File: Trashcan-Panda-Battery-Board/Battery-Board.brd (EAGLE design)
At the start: 89.9 x 38.6 mm, 4 parts, among them J1 B2B-PH-SM4-TB(LF)(SN)

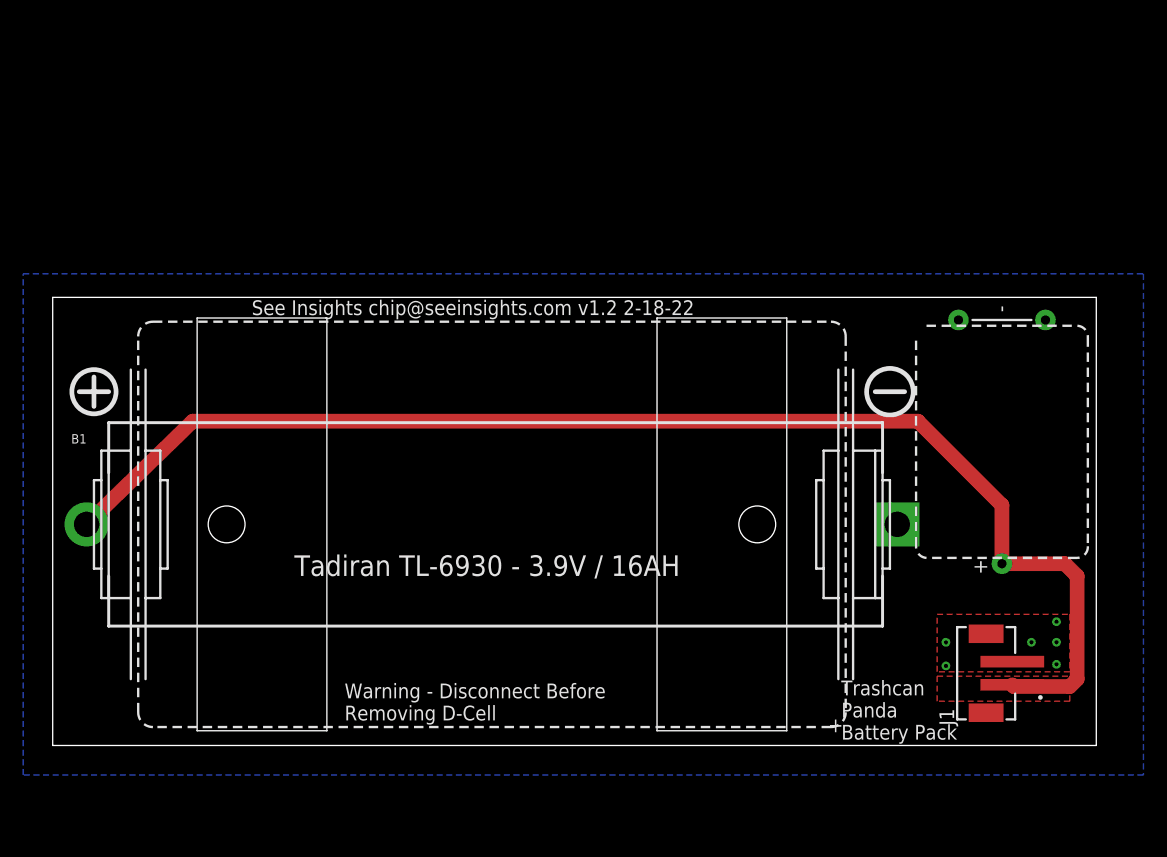
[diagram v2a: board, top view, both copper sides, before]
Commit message: Added PTC
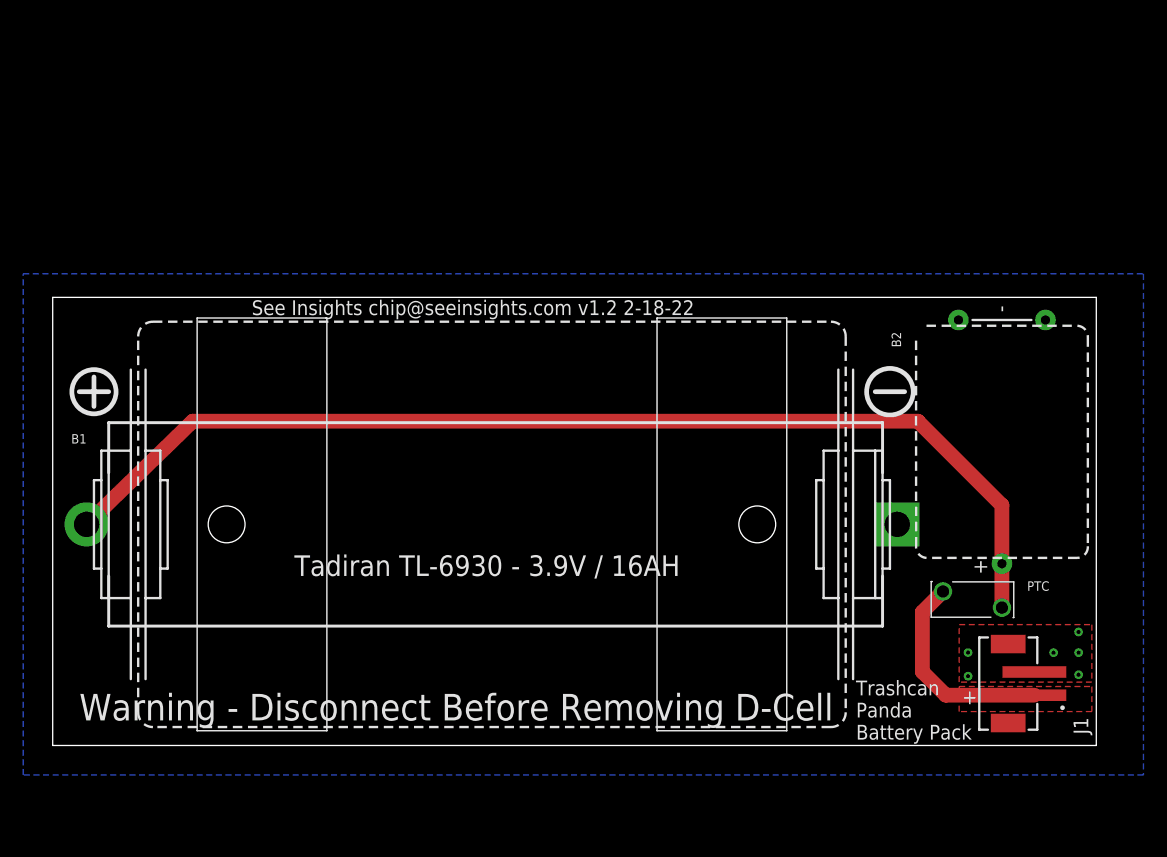
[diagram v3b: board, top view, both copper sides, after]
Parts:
- added PTC: RUSBF120, Battery-Board:PTC-RUSBF120
- moved J1 2.10 mm to (84.6, 5.33)
- renumbered U$1 to B2
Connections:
- new net V-OUT: J1.1, PTC.2
- net VCC: now also PTC.1; no longer J1.1
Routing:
- net V-OUT: track 0.00 -> 18.1 mm
- net VCC: track 112.2 -> 94.3 mm
- added copper zone on layer 1, net V-OUT
- removed copper zone on layer 1, net VCC
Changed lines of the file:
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@@
 <wire x1="89.916" y1="38.608" x2="0" y2="38.608" width="0" layer="20"/>
 <wire x1="0" y1="38.608" x2="0" y2="0" width="0" layer="20"/>
-<text x="67.945" y="0.508" size="1.27" layer="21">Trashcan
+<text x="69.215" y="0.508" size="1.27" layer="21">Trashcan
 Panda
 Battery Pack</text>
-<text x="25.146" y="2.159" size="1.27" layer="21">Warning - Disconnect Before
-Removing D-Cell</text>
+<text x="2.286" y="2.159" size="2.286" layer="21">Warning - Disconnect Before Removing D-Cell</text>
 <text x="17.145" y="37.084" size="1.27" layer="21">See Insights chip@seeinsights.com v1.2 2-18-22</text>
 <text x="20.828" y="14.605" size="1.778" layer="21">Tadiran TL-6930 - 3.9V / 16AH</text>
-<text x="66.802" y="1.143" size="1.27" layer="21">+</text>
+<text x="78.359" y="3.556" size="1.27" layer="21">+</text>
 </plain>
 <attributes>
@@
 <attribute name="PRICE" value="None" x="37.846" y="19.05" size="1.778" layer="27" display="off"/>
 <attribute name="PURCHASE-URL" value="https://pricing.snapeda.com/search/part/2226/?ref=eda" x="37.846" y="19.05" size="1.778" layer="27" display="off"/>
-<attribute name="VALUE" x="36.57376875" y="8.2444" size="0.8135125" layer="27" ratio="10"/>
-</element>
-<element name="J1" library="Custom Components" package="JST_B2B-PH-SM4-TB(LF)(SN)" value="B2B-PH-SM4-TB(LF)(SN)" x="82.677" y="6.223" smashed="yes" rot="R90">
-<attribute name="DESCRIPTION" value=" Connector Header Surface Mount 2 position 0.079 (2.00mm) " x="82.677" y="6.223" size="1.778" layer="27" rot="R90" display="off"/>
-<attribute name="DIGI-KEY_PART_NUMBER" value="455-1734-1-ND" x="82.677" y="6.223" size="1.778" layer="27" rot="R90" display="off"/>
-<attribute name="MF" value="JST Sales" x="82.677" y="6.223" size="1.778" layer="27" rot="R90" display="off"/>
-<attribute name="MP" value="B2B-PH-SM4-TB(LF)(SN)" x="82.677" y="6.223" size="1.778" layer="27" rot="R90" display="off"/>
-<attribute name="NAME" x="77.67053125" y="1.71718125" size="1.271640625" layer="25" rot="R90"/>
-<attribute name="PACKAGE" value="None" x="82.677" y="6.223" size="1.778" layer="27" rot="R90" display="off"/>
-<attribute name="PURCHASE-URL" value="https://pricing.snapeda.com/search/part/B2B-PH-SM4-TB(LF)(SN)/?ref=eda" x="82.677" y="6.223" size="1.778" layer="27" rot="R90" display="off"/>
-</element>
-<element name="U$1" library="Battery-Board" package="HLC-1520A/TP" value="HLC-1520A/TP" x="81.788" y="26.162" smashed="yes" rot="R90">
+</element>
+<element name="J1" library="Custom Components" package="JST_B2B-PH-SM4-TB(LF)(SN)" value="B2B-PH-SM4-TB(LF)(SN)" x="84.582" y="5.334" smashed="yes" rot="R90">
+<attribute name="DESCRIPTION" value=" Connector Header Surface Mount 2 position 0.079 (2.00mm) " x="84.582" y="5.334" size="1.778" layer="27" rot="R90" display="off"/>
+<attribute name="DIGI-KEY_PART_NUMBER" value="455-1734-1-ND" x="84.582" y="5.334" size="1.778" layer="27" rot="R90" display="off"/>
+<attribute name="MF" value="JST Sales" x="84.582" y="5.334" size="1.778" layer="27" rot="R90" display="off"/>
+<attribute name="MP" value="B2B-PH-SM4-TB(LF)(SN)" x="84.582" y="5.334" size="1.778" layer="27" rot="R90" display="off"/>
+<attribute name="NAME" x="89.22753125" y="0.95518125" size="1.271640625" layer="25" rot="R90"/>
+<attribute name="PACKAGE" value="None" x="84.582" y="5.334" size="1.778" layer="27" rot="R90" display="off"/>
+<attribute name="PURCHASE-URL" value="https://pricing.snapeda.com/search/part/B2B-PH-SM4-TB(LF)(SN)/?ref=eda" x="84.582" y="5.334" size="1.778" layer="27" rot="R90" display="off"/>
+</element>
+<element name="B2" library="Battery-Board" package="HLC-1520A/TP" value="HLC-1520A/TP" x="81.788" y="26.162" smashed="yes" rot="R90">
 <attribute name="MFG" value="Tadiran" x="81.788" y="26.162" size="1.778" layer="27" rot="R90" display="off"/>
 <attribute name="MPN" value="HLC-1520A/TP" x="81.788" y="26.162" size="1.778" layer="27" rot="R90" display="off"/>
-<attribute name="VALUE" x="84.9736" y="22.34976875" size="0.8128" layer="27" rot="R90"/>
+<attribute name="NAME" x="72.2851" y="35.6311" size="0.8128" layer="25" rot="R270"/>
 </element>
 <element name="FRAME1" library="SparkFun-Aesthetics" library_urn="urn:adsk.eagle:library:507" package="CREATIVE_COMMONS" package3d_urn="urn:adsk.eagle:package:37121/1" value="FRAME-LETTER" x="19.05" y="-16.51" smashed="yes"/>
+<element name="PTC" library="Battery-Board" package="PTC-RUSBF120" value="RUSBF120" x="79.248" y="12.573" smashed="yes" rot="R180">
+<attribute name="MPN" value="RUSBF120" x="79.248" y="12.573" size="1.778" layer="27" rot="R180" display="off"/>
+<attribute name="NAME" x="85.87331875" y="14.1412" size="0.8128" layer="25" rot="R180"/>
+<attribute name="WEB" value="https://www.littelfuse.com/~/media/electronics/product_specifications/resettable_ptcs/littelfuse_ptc_rusbf120_product_specification.pdf.pdf" x="79.248" y="12.573" size="1.778" layer="27" rot="R180" display="off"/>
+</element>
 </elements>
 <signals>
 <signal name="VCC">
-<contactref element="J1" pad="1"/>
-<contactref element="U$1" pad="+"/>
+<contactref element="B2" pad="+"/>
 <contactref element="B1" pad="+"/>
 <wire x1="2.921" y1="19.05" x2="12.065" y2="27.94" width="1.27" layer="1"/>
 <wire x1="12.065" y1="27.94" x2="74.549" y2="27.94" width="1.27" layer="1"/>
-<polygon width="0.1524" layer="1">
-<vertex x="76.2" y="5.969"/>
-<vertex x="87.63" y="5.969"/>
-<vertex x="87.63" y="3.81"/>
-<vertex x="76.2" y="3.81"/>
-</polygon>
-<wire x1="81.788" y1="15.662" x2="87.208" y2="15.662" width="1.27" layer="1"/>
-<wire x1="87.208" y1="15.662" x2="88.265" y2="14.605" width="1.27" layer="1"/>
-<wire x1="88.265" y1="14.605" x2="88.265" y2="5.715" width="1.27" layer="1"/>
-<wire x1="88.265" y1="5.715" x2="87.63" y2="5.08" width="1.27" layer="1"/>
-<wire x1="87.63" y1="5.08" x2="82.82" y2="5.08" width="1.27" layer="1"/>
-<wire x1="82.82" y1="5.08" x2="82.677" y2="5.223" width="1.27" layer="1"/>
 <wire x1="74.549" y1="27.94" x2="81.788" y2="20.701" width="1.27" layer="1"/>
 <wire x1="81.788" y1="20.701" x2="81.788" y2="15.662" width="1.27" layer="1"/>
+<contactref element="PTC" pad="1"/>
+<wire x1="81.788" y1="15.662" x2="81.788" y2="11.873" width="1.27" layer="1"/>
 </signal>
 <signal name="GND">
 <contactref element="J1" pad="2"/>
-<contactref element="U$1" pad="--"/>
-<contactref element="U$1" pad="-"/>
+<contactref element="B2" pad="--"/>
+<contactref element="B2" pad="-"/>
 <contactref element="B1" pad="-"/>
 <polygon width="0.1524" layer="1">
-<vertex x="76.2" y="11.303"/>
-<vertex x="87.63" y="11.303"/>
-<vertex x="87.63" y="6.35"/>
-<vertex x="76.2" y="6.35"/>
+<vertex x="78.105" y="10.414"/>
+<vertex x="89.535" y="10.414"/>
+<vertex x="89.535" y="5.461"/>
+<vertex x="78.105" y="5.461"/>
 </polygon>
-<via x="86.487" y="6.985" extent="1-16" drill="0.35"/>
-<via x="76.962" y="8.89" extent="1-16" drill="0.35"/>
-<via x="84.328" y="8.89" extent="1-16" drill="0.35"/>
-<via x="76.962" y="6.858" extent="1-16" drill="0.35"/>
-<via x="86.487" y="10.668" extent="1-16" drill="0.35"/>
-<via x="86.487" y="8.89" extent="1-16" drill="0.35"/>
+<via x="88.392" y="6.096" extent="1-16" drill="0.35"/>
+<via x="78.867" y="8.001" extent="1-16" drill="0.35"/>
+<via x="86.233" y="8.001" extent="1-16" drill="0.35"/>
+<via x="78.867" y="5.969" extent="1-16" drill="0.35"/>
+<via x="88.392" y="9.779" extent="1-16" drill="0.35"/>
+<via x="88.392" y="8.001" extent="1-16" drill="0.35"/>
 <polygon width="0.4064" layer="16">
 <vertex x="-2.54" y="40.64"/>
@@
 <vertex x="-2.54" y="-2.54"/>
 </polygon>
-<wire x1="78.038" y1="36.662" x2="85.538" y2="36.662" width="0" layer="19" extent="1-1"/>
-<wire x1="72.771" y1="19.05" x2="78.038" y2="36.662" width="0" layer="19" extent="1-1"/>
-<wire x1="76.962" y1="8.89" x2="72.771" y2="19.05" width="0" layer="19" extent="1-1"/>
+</signal>
+<signal name="V-OUT">
+<contactref element="PTC" pad="2"/>
+<contactref element="J1" pad="1"/>
+<wire x1="76.708" y1="13.273" x2="74.93" y2="11.495" width="1.27" layer="1"/>
+<wire x1="74.93" y1="11.495" x2="74.93" y2="6.35" width="1.27" layer="1"/>
+<wire x1="74.93" y1="6.35" x2="76.946" y2="4.334" width="1.27" layer="1"/>
+<wire x1="76.946" y1="4.334" x2="84.582" y2="4.334" width="1.27" layer="1"/>
+<polygon width="0.1524" layer="1">
+<vertex x="78.105" y="5.08"/>
+<vertex x="89.535" y="5.08"/>
+<vertex x="89.535" y="2.921"/>
+<vertex x="78.105" y="2.921"/>
+</polygon>
 </signal>
 </signals>
